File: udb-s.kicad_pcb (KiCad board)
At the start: 4 copper layers, 40 x 9 mm, 11 parts, among them J1 TYPE-C-31-M-12, J2 78171-0004, U1 TPD4E05U06DQAR

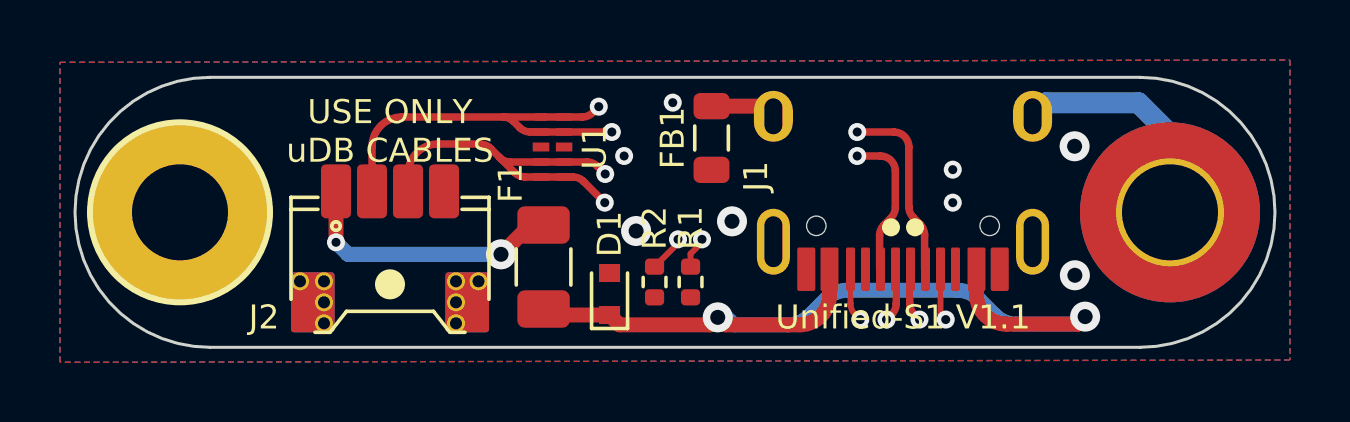
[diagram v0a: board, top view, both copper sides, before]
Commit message: mods for jst-sh
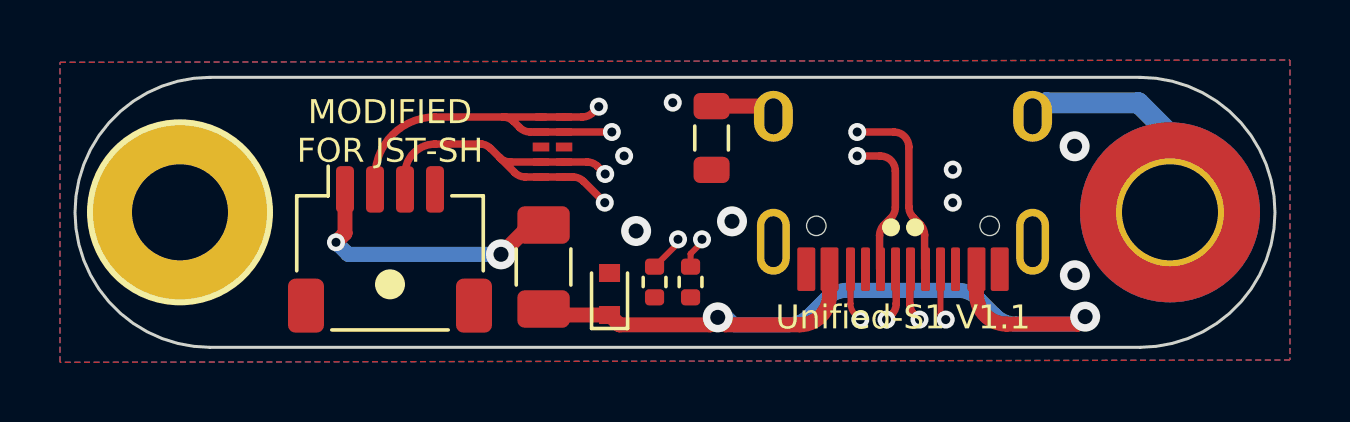
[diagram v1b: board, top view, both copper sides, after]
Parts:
- J2: footprint locallib:PicoEZMate-Reinforced-Lite -> Connector_JST:JST_SH_SM04B-SRSS-TB_1x04-1MP_P1.00mm_Horizontal
- moved J2 0.27 mm to (122.0, 96.2)
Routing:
- net D-: track 49.5 -> 48.9 mm
- net D+: track 49.6 -> 50.2 mm
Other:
- board text added: "MODIFIED FOR JST-SH"
- board text removed: "USE ONLY uDB CABLES"

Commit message: v2
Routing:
- net GND: vias 6 -> 18
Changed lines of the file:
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@@
   )
   (paper "A4")
+  (title_block
+    (rev "v2")
+  )
   (layers
     (0 "F.Cu" signal)
@@
   )
   (segment (start 135.85 96.8975) (end 135.85 97.327913) (width 0.2) (layer "F.Cu") (net 1))
+  (via (at 119.5 98.71) (size 0.5) (drill 0.3) (layers "F.Cu" "B.Cu") (net 1))
+  (via (at 118.9 97.51) (size 0.5) (drill 0.3) (layers "F.Cu" "B.Cu") (net 1))
   (via (at 129.80375 93.1225) (size 0.6) (drill 0.3) (layers "F.Cu" "B.Cu") (free) (net 1))
+  (via (at 124.5 98.11) (size 0.5) (drill 0.3) (layers "F.Cu" "B.Cu") (net 1))
+  (via (at 124.5 97.51) (size 0.5) (drill 0.3) (layers "F.Cu" "B.Cu") (net 1))
   (via (at 133.4 95.3) (size 1) (drill 0.5) (layers "F.Cu" "B.Cu") (free) (net 1))
+  (via (at 125.1 97.51) (size 0.5) (drill 0.3) (layers "F.Cu" "B.Cu") (net 1))
   (via (at 144.829639 97.098274) (size 1) (drill 0.5) (layers "F.Cu" "B.Cu") (free) (net 1))
+  (via (at 119.5 97.51) (size 0.5) (drill 0.3) (layers "F.Cu" "B.Cu") (net 1))
+  (via (at 119.5 98.11) (size 0.5) (drill 0.3) (layers "F.Cu" "B.Cu") (net 1))
+  (via (at 124.5 98.71) (size 0.5) (drill 0.3) (layers "F.Cu" "B.Cu") (net 1))
   (via (at 130.20375 95.6225) (size 1) (drill 0.5) (layers "F.Cu" "B.Cu") (free) (net 1))
+  (via (at 125.1 98.11) (size 0.5) (drill 0.3) (layers "F.Cu" "B.Cu") (net 1))
   (via (at 131.425 91.34375) (size 0.6) (drill 0.3) (layers "F.Cu" "B.Cu") (free) (net 1))
   (via (at 144.820324 92.798274) (size 1) (drill 0.5) (layers "F.Cu" "B.Cu") (free) (net 1))
+  (via (at 118.9 98.71) (size 0.5) (drill 0.3) (layers "F.Cu" "B.Cu") (net 1))
+  (via (at 125.1 98.71) (size 0.5) (drill 0.3) (layers "F.Cu" "B.Cu") (net 1))
+  (via (at 118.9 98.11) (size 0.5) (drill 0.3) (layers "F.Cu" "B.Cu") (net 1))
   (segment (start 129.31875 98.4225) (end 127.31875 98.4225) (width 0.5) (layer "F.Cu") (net 2))
   (segment (start 129.646751 98.750501) (end 129.31875 98.4225) (width 0.5) (layer "F.Cu") (net 2))
